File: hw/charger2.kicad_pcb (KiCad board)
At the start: 2 copper layers, 100 x 60 mm, 140 parts, among them J2 Conn_01x08, J3 Conn_01x08, J4 4.5V Power Supply, J5 External ADS1115, J6 Temp, J7 Temp, Q10 AO3400, Q11 AO3400, Q12 AO3400, Q13 AO3400, Q14 AO3400, Q15 AO3400, Q16 AO3400, Q17 AO3400, Q2 AO3400, Q3 AO3400, Q4 AO3400, Q5 AO3400, Q6 AO3400, Q7 AO3400, Q8 AO3400, Q9 AO3400, SW1 Rotary_Encoder_Switch, U1 4050, U10 TP4056, U12 MCP23017_SS, U15 4052, U17 TP4056, U18 TP4056, U19 TP4056, U2 MCP23017_SS, U20 TP4056, U23 ADS1115IDGS, U3 ILI9341 2.2" Display, U5 4052, U7 TP4056, U8 TP4056, U9 TP4056

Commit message: multiple changes
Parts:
- added C25: 100n, Capacitor_SMD:C_0805_2012Metric_Pad1.15x1.40mm_HandSolder, F.Cu at (150.1, 90.1)
- added C27: 100n, Capacitor_SMD:C_0805_2012Metric_Pad1.15x1.40mm_HandSolder, F.Cu at (149.3, 110.8)
- added D1: SS34, Diode_SMD:D_SMA, F.Cu at (132.6, 92.1)
- U1: value 4050 -> 74HC4050
- U3: value ILI9341 2.2" Display -> 2.2" SPI display
- XA1: value Arduino_Nano_Socket -> Arduino Nano
- moved U1 0.10 mm to (201.1, 98.0)
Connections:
- U15 pad 16: +5V -> +5VA
- U5 pad 16: +5V -> +5VA
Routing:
- net +5VA: track 36.8 -> 70.8 mm, vias 3 -> 7
- net +5V: track 280.7 -> 276.9 mm, vias 19 -> 16
- net GND: track 295.1 -> 298.7 mm
- net /quadcharger2/Y2: track 24.4 -> 27.7 mm
- net VCC: track 336.3 -> 338.5 mm, vias 52 -> 54
- net /quadcharger2/sheet5DC5D9EA/CHRG: track 27.6 -> 26.5 mm
- net Net-(U12-Pad26): track 34.5 -> 33.7 mm
- net /quadcharger2/sheet5DC5DB5C/CHRG: track 43.5 -> 42.7 mm
- net Net-(U12-Pad25): track 34.3 -> 33.5 mm
- net /quadcharger2/sheet5DC5DB5C/CE: track 40.0 -> 39.2 mm

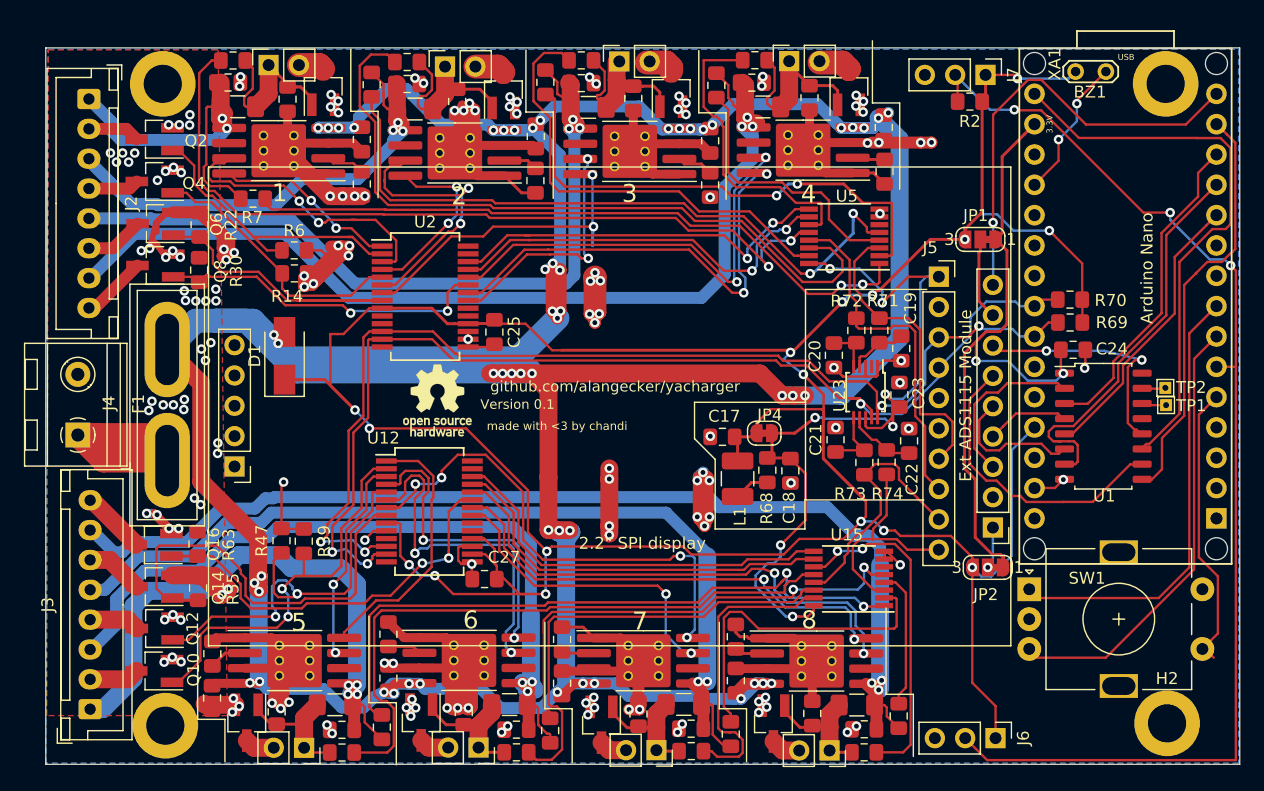
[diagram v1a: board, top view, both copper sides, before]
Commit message: fix mux enable pin, reroute some traces
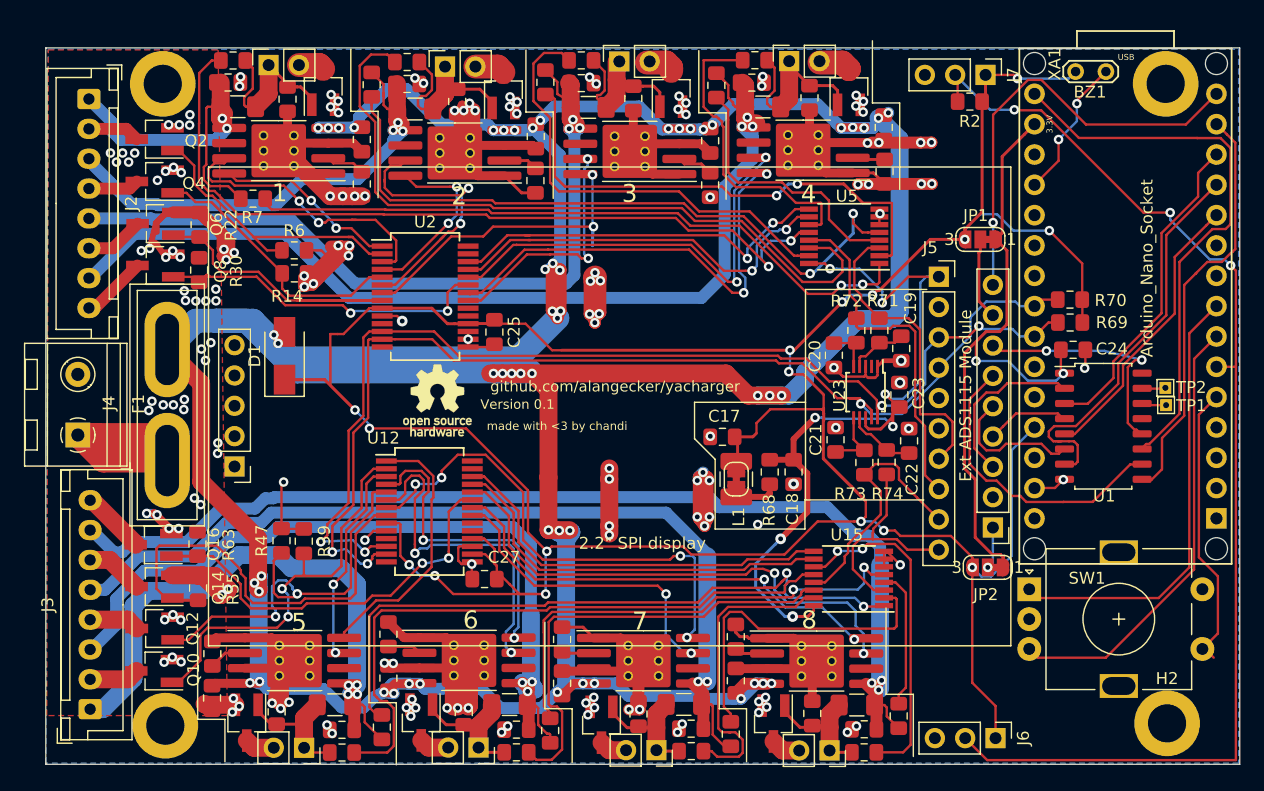
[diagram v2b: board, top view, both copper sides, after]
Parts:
- R68: value 4 -> 22
- XA1: value Arduino Nano -> Arduino_Nano_Socket
- moved JP4 4.51 mm to (170.4, 102.4), turned to 270 degrees
- moved C18 0.29 mm to (175.2, 101.8)
- moved R68 0.25 mm to (173.2, 101.8)
- moved L1 0.12 mm to (170.4, 102.4)
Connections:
- J5 pad 6: Net-(J5-Pad6) -> (no net)
- JP4 pad 2: +5VA -> Net-(JP4-Pad2)
- L1 pad 1: Net-(L1-Pad1) -> Net-(JP4-Pad2)
- R68 pad 2: Net-(L1-Pad1) -> Net-(JP4-Pad2)
- U10 pad 6: Net-(U10-Pad6) -> (no net)
- U12 pad 10: Net-(U12-Pad10) -> GND
- U12 pad 11: Net-(U12-Pad11) -> (no net)
- U12 pad 14: Net-(U12-Pad14) -> (no net)
- U12 pad 19: Net-(U12-Pad19) -> (no net)
- U12 pad 20: Net-(U12-Pad20) -> (no net)
- U12 pad 27: Net-(U12-Pad27) -> (no net)
- U12 pad 28: Net-(U12-Pad28) -> (no net)
- U15 pad 6: Net-(U15-Pad6) -> GND
- U17 pad 6: Net-(U17-Pad6) -> (no net)
- U18 pad 6: Net-(U18-Pad6) -> (no net)
- U19 pad 6: Net-(U19-Pad6) -> (no net)
- U2 pad 10: Net-(U2-Pad10) -> GND
- U2 pad 11: Net-(U2-Pad11) -> (no net)
- U2 pad 14: Net-(U2-Pad14) -> (no net)
- U2 pad 19: Net-(U2-Pad19) -> (no net)
- U2 pad 20: Net-(U2-Pad20) -> (no net)
- U2 pad 27: Net-(U2-Pad27) -> (no net)
- U2 pad 28: Net-(U2-Pad28) -> (no net)
- U20 pad 6: Net-(U20-Pad6) -> (no net)
- U23 pad 2: Net-(U23-Pad2) -> (no net)
- U3 pad 10: Net-(U3-Pad10) -> (no net)
- U3 pad 11: Net-(U3-Pad11) -> (no net)
- U3 pad 12: Net-(U3-Pad12) -> (no net)
- U3 pad 13: Net-(U3-Pad13) -> (no net)
- U3 pad 14: Net-(U3-Pad14) -> (no net)
- U5 pad 6: Net-(U5-Pad6) -> GND
- U7 pad 6: Net-(U7-Pad6) -> (no net)
- U8 pad 6: Net-(U8-Pad6) -> (no net)
- U9 pad 6: Net-(U9-Pad6) -> (no net)
- XA1 pad A1: /MCU/A1 -> (no net)
- XA1 pad A2: /MCU/A2 -> (no net)
- XA1 pad A3: /MCU/A3 -> (no net)
- XA1 pad A6: /MCU/A6 -> (no net)
- XA1 pad A7: /MCU/A7 -> (no net)
- XA1 pad AREF: Net-(XA1-PadAREF) -> (no net)
- XA1 pad D0: Net-(XA1-PadD0) -> (no net)
- XA1 pad D1: Net-(XA1-PadD1) -> (no net)
- XA1 pad D6: /MCU/D6 -> (no net)
- XA1 pad D7: /MCU/D7 -> (no net)
- XA1 pad RST1: Net-(XA1-PadRST1) -> (no net)
- XA1 pad RST2: Net-(XA1-PadRST2) -> (no net)
- XA1 pad VIN: Net-(XA1-PadVIN) -> (no net)
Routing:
- net GND: track 298.7 -> 310.3 mm, vias 158 -> 165
- net Net-(JP4-Pad2): track 0.00 -> 4.53 mm
- net Net-(L1-Pad1): track 2.98 -> 0.00 mm
- net +5VA: track 70.8 -> 68.6 mm
- net Net-(U12-Pad10): track 2.15 -> 0.00 mm, vias 1 -> 0
- net /quadcharger2/sheet5DC5DB5C/CE: track 39.2 -> 38.0 mm
- net VCC: track 338.5 -> 337.6 mm
- net +5V: track 276.9 -> 277.7 mm
